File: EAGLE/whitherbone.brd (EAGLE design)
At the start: 86.4 x 54.6 mm, 222 parts, among them IC1 A4983, IC12 TPS2051BDGN, IC13 SN74AUC1G74, IC14 TPD4S012DRY, IC15 TPD4S012DRY, IC17 SN74LVC2G241DCUR, IC2 SN74LVC1G07DCK, IC4 7805T, IC7 IP4283CZ10-TBR, IC8 IP4283CZ10-TBR, IC9 TDA19988BHN/C1,557, J1 1-1747981-1, Q2 32.768kHz, Q4 24 MHz, T1 BSS138W-7-F, T3 BSS138W-7-F, T4 BSS138W-7-F, U1 OSD3358-512M-BSM, U2 SN74AHCT125PW, X2 SCHA5B0200, X4 10118192-0001LF

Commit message: Use version from Seeed
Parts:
- removed ANT1, ANT2: U.FL-R-SMT-1(10), GHI-Connectors:U.FL-R-SMT-1
- removed BT, BT1, PWR, USR0, USR1, USR2, USR3, WL: LTST-C191TBKT, GHI-BasicComponents:0603-LED
- removed FB4: 0.1 Ohm, 0805, GHI-BasicComponents:0805-RESISTOR
- removed IC13: SN74AUC1G74, GHI-IC:SM8-8(TI)
- removed IC14: TPD4S012DRY, GHI-IC:SON-6(TI)-DRY
- removed IC17: SN74LVC2G241DCUR, GHI-IC:VSSOP8(TI)
- removed IC2: SN74LVC1G07DCK, GHI-IC:SC70(TI-DCK)
- removed IC4: 7805T, linear:TO220H
- removed IC7, IC8: IP4283CZ10-TBR, GHI-IC:SOT1176-1(NXP)
- removed IC9: TDA19988BHN/C1,557, GHI-IC:SOT804-4(NXP)
- removed OSC1: ASDMB-24.576MHZ-LC-T, GHI2:OSCILLATOR-2.5X2.0-BBB
- removed OSC2: NZ2520SB-32.768KHZ-NSA3534C, GHI-IC:NZ2520S
- removed POWER, RESET: MINI_PUSHBUTTON, GHI2:MINI_PUSHBUTTON
- removed Q2: 32.768kHz, GHI2:CRYSTAL_3.2X1.5
- removed Q4: 24 MHz, GHI2:CRYSTAL_5X3.2MM
- removed R101: 10k, rcl:R0402
- removed R115, R118: 1.5k, 1%, rcl:R0402
- removed R119, R121: 10k, 1%, rcl:R0402
- removed R120: 27k, 1%, rcl:R0402
- removed R123, R76: 100k, 1%, rcl:R0402
- removed R23: 20K, SparkFun:0402-RES
- removed X1: (no value), GHI-Headers:TH-1X6
- removed X12: (no value), GHI-Connectors:PJ-102B_POWER_CON
- removed X3: (no value), GHI2:USB_HOST_HORIZONTAL_W/CHASSIS_GND
- removed X4: 10118192-0001LF, GHI-Connectors:10118192-0001LF(MICRO-USB-B-AMPHENOL-FCI)
- added ANT3, ANT4: (no value), Connector-new:U-FL3P-SMD-2.6X2.6X1.0MM
- added C22: 0.1uF, 6.3V, Discrete-new:C0402
- added C25, C26: 47pF, Discrete-new:C0402
- added C45, C65, C69, C76: 100nF, Discrete-new:C0402
- added C66: .1uF, 6.3V, Discrete-new:C0402
- added C67: 22nF, Discrete-new:C0402
- added C68: 100nF, Discrete-new:C0603
- added C70, C71: 47uF 25V, Discrete-new:ELECTRO-SMD-C-6MM
- added C72: 220nF, Discrete-new:C0402
- added C73: 100nF, Discrete-new:C0805
- added C74: DNI, Discrete-new:C0402
- added C75: 1uF 10V, Discrete-new:C0402
- added C77, C78, C80, C82, C83, C84: 10uF, Discrete-new:C0805
- added C79: 22uF, Discrete-new:ELECTRO-SMD-B-4.8MM
- added C81: 22uF 16V, Discrete-new:C1206
- added D10, D12, D13, D2, D3: DF2S6.8FS, Discrete-new:SOD-923
- added D11, D4, D5, D6, D7, D8, D9: (no value), Discrete-new:LED-0603
- added J2: (no value), Connector-new:H2-2.54
- added J3: 6p-2.54, OSD3358-BSP Ref Design:H6-2.54
- added J4: ST-HD-010, template:HDMI19P-0.5-15X12.15X6.18MM
- added J5: (no value), Connector-new:MICRO-SD9+4P-SMD-16.1X14.5X1.85MM
- added J6: DC Power Jack, For_Test_Albert:DC-404
- added J7: (no value), Connector-new:H4-3.5-14.0X7.0MM
- added J8: (no value), Connector-new:MICRO-USB5+5P-SMD-0.65-7.2X5.06MM
- added L1, L4: WPN201610MR47MT, Discrete-new:L201610
- added L2: 10uH, Discrete-new:L5040S
- added Q1: MMBT2907, Discrete-new:SOT-323
- added R106, R107, R108, R109, R112, R113: 33R, Discrete-new:R0402
- added R30, R51: 0R, Discrete-new:R0402
- added R31, R44: 22R, Discrete-new:R0402
- added R33: 0, 1%, Discrete-new:R0402
- added R33333, R48, R74, R77, R79, R97: 10k, Discrete-new:R0402
- added R36, R38: 1.5K, 1%, Discrete-new:R0402
- added R40: 5.6K 1%, Discrete-new:R0402
- added R41, R42: 100k 1%, Discrete-new:R0402
- added R45, R46: 2k, Discrete-new:R0402
- added R47: 33k, Discrete-new:R0402
- added R49, R50: 10K, Discrete-new:R0402
- added R54: 10k, 1%, Discrete-new:R0402
- added R59, R81, R82, R83: 100K, 1%, Discrete-new:R0402
- added R84: 3.3k, Discrete-new:R0402
- added R86, R89, R91: 10K, 1%, Discrete-new:R0402
- added R93: 510R 1%, Discrete-new:R0402
- added R94: 24k, Discrete-new:R0402
- added SW1, SW2: (no value), Discrete-new:BUTTON4P-SMD-4.5X3.2X2.5MM
- added TP11, TP21, TP22, TP23, TP24, TP3, TP4: TPB0,65, OSD3358-BSP Ref Design:TP_B0,65
- added TP20, TP25, TP27, TP28, TP29, TP30, TP31, TP32, TP9: (no value), Discrete-new:TP-D45MIL
- added TP26, TP5, TP6, TP7, TP8: TESTPAD/W_HOLE_1X1, OSD3358-BSP Ref Design:TESTPAD/W_HOLE_1X1
- added TP33: TPPAD1-13, testpad:P1-13
- added U10: (no value), IC-new:SOT-353
- added U11, U9: ESD-RCLAMP0524P, Discrete-new:ESD10P-0.5-2.5X1X0.58MM
- added U12: TL431, IC-new:SOT-23
- added U13: (no value), IC-new:5P-SMD-2X1.2X1MM
- added U3: MP1496DJ-LF-2, IC-new:SOT-23-8
- added U4: APX811, IC-new:SOT143-R
- added U5, U8: ETA3410, IC-new:DFN8G-0.5-2X2MM
- added U6: SN74LVC2G241_DCU_8, OSD3358-BSP Ref Design:DCU8
- added U7: IT66121FN, IC-new:QFN64-0.5-9X9MM
- added VIN: (no value), discrete:TP_4545
- added VR1: EVM3GSX50B14, Discrete-new:ADJR3-SMD-3.6X3.3MM
- added Y1: ABS07-32.768KHZ-T, OSD3358-BSP Ref Design:CRYSTAL_3.2X1.5
- added Y2: 7A-24.000MAAJ-T, OSD3358-BSP Ref Design:CRYSTAL-TXC-7A
- C1: value 10uF,10V -> 10uF; device rcl:C0603K -> Discrete-new:C0805
- C10: value .1uf -> 0.1uF, 6.3V; device SparkFun:0402-CAP -> Discrete-new:C0402
- C11: value 47uF DNP -> TLJB227M006R0500; device rcl:CT3528 -> Discrete-new:AVX-B
- C12: value 1uF,10V -> 18pF, 50V; device Seeed-Capacitor:C0402 -> Discrete-new:C0402
- C13, C14: value .1uf -> 100nF; device SparkFun:0402-CAP -> Discrete-new:C0402
- C15, C18: value .1uf -> 10uF; device SparkFun:0402-CAP -> Discrete-new:C0805
- C16: value 2.2uF, 6.3V -> 100nF; device rcl:C0603K -> Discrete-new:C0402
- C17: value .22uF -> 100nF; device SparkFun:0402-CAP -> Discrete-new:C0402
- C19: value 1uF,10V -> 10uF; device Seeed-Capacitor:C0402 -> Discrete-new:C0805
- C2: value .1uF, 6.3V -> DNI; device rcl:C0402K -> Discrete-new:C0402
- C20: value 10uF, 6.3V -> 10uF; device rcl:C0603K -> Discrete-new:C0805
- C21: value 1uF,10V -> 10uF, 10V; device Seeed-Capacitor:C0402 -> Discrete-new:C0805
- C23: value 47uF DNP -> 47pF; device rcl:CT3528 -> Discrete-new:C0402
- C24: value .1uF, 6.3V -> 47pF; device rcl:C0402K -> Discrete-new:C0402
- C27, C28, C29, C30, C31, C32, C33, C34, C35, C36, C37, C38: value 47pF, 6.3V -> 47pF; device rcl:C0402K -> Discrete-new:C0402
- C3, C6: value 18pF, 50V -> 0.1uF, 6.3V; device rcl:C0402K -> Discrete-new:C0402
- C39, C40, C41: value 47pF, 6.3V -> 10uF; device rcl:C0402K -> Discrete-new:C0805
- C4, C5: device rcl:C0402K -> Discrete-new:C0402
- C42: value 47pF, 6.3V -> 1uF; device rcl:C0402K -> Discrete-new:C0402
- C43, C44, C47, C48, C49, C50, C51, C63: value .1uF, 6.3V -> 100nF; device rcl:C0402K -> Discrete-new:C0402
- C46, C60: value 10pF -> 100nF; device rcl:C0402K -> Discrete-new:C0402
- C52, C53: value .1uF, 6.3V -> 47uF DNP; device rcl:C0402K -> Discrete-new:C1206
- C54: value 2.2uF, 6.3V -> 220uF; device rcl:C0603K -> Discrete-new:AVX-E
- C55, C56: value 2.2uF, 6.3V -> 10pF; device rcl:C0603K -> Discrete-new:C0402
- C57: value 2.2uF, 6.3V -> 10uF; device rcl:C0603K -> Discrete-new:C0805
- C58: value .1uF, 6.3V -> 1uF; device rcl:C0402K -> Discrete-new:C0402
- C59: value .1uF, 6.3V -> DNP; device rcl:C0402K -> Discrete-new:C0402
- C61: value 10uF, 6.3V -> 100nF; device rcl:C0603K -> Discrete-new:C0402
- C62: value 220uF 6.3V -> 1uF; device rcl:D/7343-31W -> Discrete-new:C0603
- C64: value 1uF, 6.3V -> 1uF; device rcl:C0402K -> Discrete-new:C0402
- C7: value 47uF,50V -> 18pF, 50V; device resistor:PANASONIC_F -> Discrete-new:C0402
- C8: value 1uF -> 1nF; device rcl:C0402K -> Discrete-new:C0402
- C9: value 100nF,50V -> 0.1uF, 6.3V; device Seeed-Capacitor:C0805 -> Discrete-new:C0402
- D1: value RB751V40,115 -> (none); device GHI-BasicComponents:SOD323(NXP)REFLOW -> Discrete-new:LED-0603
- F1: value 1206L025YR -> 100mA MF-FSMF010X; device inductor-neosid:SM-1206 -> Discrete-new:F0603
- FB1, FB6, FB7, FB8: value 1k BLM15AG102SN1D -> BLM15PD121SN1D; device rcl:R0402 -> Discrete-new:L0402
- FB2: value 2.5k Ohm (BLM18BD252SN1D) -> BLM15PD121SN1D; device GHI-BasicComponents:0805-RESISTOR -> Discrete-new:L0402
- FB3: device GHI-BasicComponents:0805-RESISTOR -> Discrete-new:L0805
- FB5: value 1k BLM15AG102SN1D -> 0.1 Ohm, 0805; device rcl:R0402 -> Discrete-new:L0805
- FUD1, FUD2, FUD3, FUD4, FUD5, FUD6: device GHI:FIDUCIAL_40MIL -> OSD3358-BSP Ref Design:FIDUCIAL_40MIL
- IC1: device SparkFun:QFN-28-5MM -> IC-new:QFN-28-5MM
- IC12: device GHI-IC:MSOP-POWER.PAD-8(TI) -> IC-new:MSOP8-0.65-3X3MM
- IC15: device GHI-IC:SON-6(TI)-DRY -> IC-new:SON6-0.5-1.45X1X0.55MM
- J1: value 1-1747981-1 -> (none); device 1-1747981-1:TE_1-1747981-1 -> Connector-new:H2-2.54
- MGT1, MGT2, MGT3, MGT4: device BeagleBoneBlack:MOUNTING_HOLE -> OSD3358-BSP Ref Design:MOUNTING_HOLE
- MOD1: device GHI-IC:MOC-100(TI) -> moudle-new:MODULE100P-0.7-13.5X13.2MM
- R1: value 10k, 1% -> 10K, 1%; device rcl:R0402 -> Discrete-new:R0402
- R10: value .11 -> 0, 1%; device SparkFun:R2010 -> Discrete-new:R0402
- R100, R104, R96: value 1k -> 10k; device rcl:R0402 -> Discrete-new:R0402
- R102, R103, R105, R111, R122, R124, R125: device rcl:R0402 -> Discrete-new:R0402
- R11: value 20K -> 0, 1%; device SparkFun:0402-RES -> Discrete-new:R0402
- R110: value 33 -> 33R; device rcl:R0402 -> Discrete-new:R0402
- R114: value 0, 1% -> 1k; device rcl:R0402 -> Discrete-new:R0402
- R12, R13: value 20K -> 1.5K, 1%; device SparkFun:0402-RES -> Discrete-new:R0402
- R14: value 20K -> 22k 1%; device SparkFun:0402-RES -> Discrete-new:R0402
- R140, R141, R142, R143: value 33, 5% -> 33R; device rcl:R0402 -> Discrete-new:R0402
- R15: value 20K -> 40.2K, 1%; device SparkFun:0402-RES -> Discrete-new:R0402
- R16: value 10K -> 0, 1%; device SparkFun:TRIMPOT-3MM -> Discrete-new:R0402
- R17: value .1, 0805 -> DNP; device rcl:R0805 -> Discrete-new:R0402
- R18: value .11 -> 4.75K, 1%; device SparkFun:R2010 -> Discrete-new:R0402
- R19: value 10k, 1% -> 10k; device rcl:R0402 -> Discrete-new:R0402
- R2, R3: value 10k, 1% -> 1k; device rcl:R0402 -> Discrete-new:R0402
- R20: value 20K -> 10K, 1%; device SparkFun:0402-RES -> Discrete-new:R0402
- R21: value 20K -> 499; device SparkFun:0402-RES -> Discrete-new:R0402
- R22: value 20K -> 4.75K, 1%; device SparkFun:0402-RES -> Discrete-new:R0402
- R24: value 10k, 1% -> 1M, 1%, DNI; device rcl:R0402 -> Discrete-new:R0402
- R25: value 2.49K -> 0, 1%; device SparkFun:0402-RES -> Discrete-new:R0402
- R26, R35, R37: value 0, 1% -> 1.5K, 1%; device rcl:R0402 -> Discrete-new:R0402
- R27: value 0, 1% -> 100K, 1%; device rcl:R0402 -> Discrete-new:R0402
- R28: value 47k, 1% -> 0R; device rcl:R0402 -> Discrete-new:R0402
- R29: value 22k, 1% -> 0R; device rcl:R0402 -> Discrete-new:R0402
- R32: value 10k, 1% -> 1M, 1%; device rcl:R0402 -> Discrete-new:R0402
- R34: value 22 -> 10k; device rcl:R0402 -> Discrete-new:R0402
- R39: value 0, 1% -> 10k; device rcl:R0402 -> Discrete-new:R0402
- R4: value 10k, 1% -> 22R; device rcl:R0402 -> Discrete-new:R0402
- R43: value 4.75k, 1% -> 22R; device rcl:R0402 -> Discrete-new:R0402
- R5: value 10k, 1% -> 0, 1%; device rcl:R0402 -> Discrete-new:R0402
- R52: value 4.75k, 1% -> DNP; device rcl:R0402 -> Discrete-new:R0402
- R53, R55: value 4.75k, 1% -> 100K, 1%; device rcl:R0402 -> Discrete-new:R0402
- R56: value DNP 1M, 1% -> 100K, 1%; device rcl:R0402 -> Discrete-new:R0402
- R57, R58, R61, R63, R67, R71: value 100k, 1% -> 100K, 1%; device rcl:R0402 -> Discrete-new:R0402
- R6: value 10k, 1% -> 100K, 1%, DNI; device rcl:R0402 -> Discrete-new:R0402
- R60, R62, R68: value 33, 5% -> 100K, 1%; device rcl:R0402 -> Discrete-new:R0402
- R64: value 33, 5% -> 100k; device rcl:R0402 -> Discrete-new:R0402
- R65: value 100k, 1% -> 0.1R; device rcl:R0402 -> Discrete-new:R1206
- R66: value 33, 5% -> 0.1R; device rcl:R0402 -> Discrete-new:R1206
- R69: value 100k, 1% -> 10R; device rcl:R0402 -> Discrete-new:R0402
- R7: value 10k, 1% -> 0R; device rcl:R0402 -> Discrete-new:R1206
- R70: value 33, 5% -> 10K; device rcl:R0402 -> Discrete-new:R0402
- R72: value 33, 5% -> 10k; device rcl:R0402 -> Discrete-new:R0402
- R73, R75, R78, R80: value 100k, 1% -> 10k; device rcl:R0402 -> Discrete-new:R0402
- R8: value 1M, 1% -> 1K, 1%; device rcl:R0402 -> Discrete-new:R0402
- R85: value 100k, 1% -> 2.7k 1%; device rcl:R0402 -> Discrete-new:R0402
- R87, R88: value 100k, 1% -> 10K, 1%; device rcl:R0402 -> Discrete-new:R0402
- R9: value 1k -> 100k 1%; device rcl:R0402 -> Discrete-new:R0402
- R90, R92: value 1k -> 10K, 1%; device rcl:R0402 -> Discrete-new:R0402
- R98, R99: value 10k -> 10K; device rcl:R0402 -> Discrete-new:R0402
- T1, T3, T4: device GHI Transistors:SOT-323(DIODES) -> Discrete-new:SOT-323
- TP1: value TESTPAD/W_HOLE_1X1 -> TPB0,65; device GHI2:TESTPAD/W_HOLE_1X1 -> OSD3358-BSP Ref Design:TP_B0,65
- TP12, TP13, TP14, TP15, TP16: value PTR1B1,27 -> TPB0,65; device testpad:B1,27 -> OSD3358-BSP Ref Design:TP_B0,65
- TP17, TP18, TP19: value PTR1B1,27 -> (none); device testpad:B1,27 -> Discrete-new:TP-D45MIL
- TP2: value TPPAD1-13 -> TPB0,65; device testpad:P1-13 -> OSD3358-BSP Ref Design:TP_B0,65
- U1: value OSD3358-512M-BSM -> (none); device PocketBeagle:OSD335X-BGA-256 -> IC-new:BGA256-1.27-21X21MM
- U2: value SN74AHCT125PW -> (none); device SN74AHCT125PW:SOP65P640X120-14N -> IC-new:SON6-0.5-1.45X1X0.55MM
- X2: value SCHA5B0200 -> (none); device GHI-Connectors:SCHA5B0200 -> GHI2:USB_HOST_HORIZONTAL_W/CHASSIS_GND
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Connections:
- net N$5 renamed AIN7
- removed net 12MHZ: FB6.2, IC9.27
- removed net 12M_LOOP: IC13.2, IC13.3
- removed net 32.768KHZ: MOD1.36, OSC2.3
- removed net DVI_5V: F1.1, J1.2, R115.1, R118.1
- removed net EXT_SWING: IC9.34, R119.1
- removed net HDMI.DSCL: IC9.33, J1.5, R115.2
- removed net HDMI.DSDA: IC9.32, J1.4, R118.2
- removed net HDMI_1V8: C50.1, C51.1, C52.1, C53.1, C54.1, C55.1, C56.1, C57.1, FB2.2, IC9.14, IC9.29, IC9.35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
- removed net HDMI_AUDCLK: R110.2, U1.C4
- removed net HDMI_AUDCLK_DIS#: OSC1.1, U1.T16
- removed net LCD.CLOCK: IC9.4, R34.1
- removed net LCD.D0.B0--B3: C42.1, IC9.15, R87.2, U1.G3
- removed net LCD.D1.B1--B4: C41.1, IC9.13, R85.2, U1.G2
- removed net LCD.D10.G5--G7: C32.1, IC9.64, R67.2, U1.K2
- removed net LCD.D11.R0--R3: C31.1, IC9.60, R65.2, U1.K1
- removed net LCD.D12.R1--R4: C30.1, IC9.59, R63.2, U1.L3
- removed net LCD.D13.R2--R5: C29.1, IC9.58, R61.2, U1.L2
- removed net LCD.D14.R3--R6: C28.1, IC9.57, R58.1, U1.L1
- removed net LCD.D15.R4--R7: C27.1, IC9.56, R57.2, U1.M3
- removed net LCD.D2.B2--B5: C40.1, IC9.12, R88.1, U1.G1
- removed net LCD.D3.B3--B6: C39.1, IC9.11, R80.1, U1.H3
- removed net LCD.D4.B4--B7: C38.1, IC9.10, R78.1, U1.H2
- removed net LCD.D5.G0--G2: C37.1, IC9.7, R76.1, U1.H1
- removed net LCD.D6.G1--G3: C36.1, IC9.6, R75.2, U1.J3
- removed net LCD.D7.G2--G4: C35.1, IC9.3, R73.2, U1.J2
- removed net LCD.D8.G3--G5: C34.1, IC9.2, R71.2, U1.J1
- removed net LCD.D9.G4--G6: C33.1, IC9.1, R69.2, U1.K3
- removed net LCD.ENABLE: IC9.20, R39.1
- removed net LCD.HSYNC: IC9.22, R37.1
- removed net LCD.VSYNC: IC9.21, R35.1
- removed net MCU.LCD.CLK: R34.2, U1.F1
- removed net MCU.LCD.EN: R39.2, U1.E1
- removed net MCU.LCD.HS: R37.2, U1.F2
- removed net MCU.LCD.VS: R35.2, U1.F3
- removed net N$12: C5.2, C6.2
- removed net N$4: PWR.K, R55.2
- removed net N$58: FB6.1, IC13.5
- removed net RX<-TX: IC17.3, X1.5
- removed net SD.CD: R7.1, U1.C14, X2.CD
- removed net SD.CLK: R3.1, U1.B15, X2.5
- removed net SD.CMD: R4.1, U1.B16, X2.3
- removed net SD.D0: R2.1, U1.A16, X2.7
- removed net SD.D1: R1.1, U1.A15, X2.8
- removed net SD.D2: R6.1, U1.C16, X2.1
- removed net SD.D3: R5.1, U1.C15, X2.2
- removed net SYS_RESET#: C16.1, IC2.4, R32.2, RESET.3, RESET.4, U1.R11
- removed net TEST: IC9.49, R114.2
- removed net TX->RX: IC17.2, R123.1, X1.4
- removed net TX0+: IC8.5, IC9.40, J1.13
- removed net TX0-: IC8.4, IC9.39, J1.11
- removed net TX1+: IC7.2, IC9.43, J1.16
- removed net TX1-: IC7.1, IC9.42, J1.14
- removed net TX2+: IC7.5, IC9.45, J1.19
- removed net TX2-: IC7.4, IC9.44, J1.17
- removed net TXC+: IC8.2, IC9.38, J1.10
- removed net TXC-: IC8.1, IC9.37, J1.8
- removed net UART0_RXD: IC17.6, U1.A12
- removed net UART0_TXD: IC17.5, U1.B12
- removed net USB.CLIENT.D+: IC14.1, X4.D+
- removed net USB.CLIENT.D-: IC14.2, X4.D-
- removed net USB.CLIENT.ID: IC14.3, X4.ID
- removed net USB.HOST.D+: IC15.1, X3.3
- removed net USB.HOST.D-: IC15.2, X3.2
- removed net USB_DC: C59.1, IC14.6, R26.2, U1.P9, U1.R9, U1.T9, X4.VBUS
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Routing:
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- added copper zone on layer 1, net SYS_RTC_1P8V
- added copper zone on layer 1, net SYS_VDD1_3P3V
- added copper zone on layer 1, net SYS_VDD2_3P3V
- added copper zone on layer 1, net SYS_VDD3_3P3V
- added copper zone on layer 1, net SYS_VDD_1P8V
- added copper zone on layer 1, net SYS_VOUT
- added copper zone on layer 1, net VDD_BAT
- added copper zone on layer 1, net VDD_USB_5V
- removed copper zone on layer 1, net 1.8V-WIFI
- removed copper zone on layer 1, net 3.3V-WIFI
- removed copper zone on layer 1, net 5V_IN
- removed copper zone on layer 16, net 5V_IN
- removed copper zone on layer 16, net CGND
- removed copper zone on layer 16, net DVI_5V
- removed copper zone on layer 15, net GND
- removed copper zone on layer 16, net GND
- removed copper zone on layer 15, net N$25
- removed copper zone on layer 2, net N$25
- removed copper zone on layer 16, net SELECT_5V
- removed copper zone on layer 1, net SYS_5V
- removed copper zone on layer 16, net SYS_5V
- removed copper zone on layer 1, net USB_DC
- removed copper zone on layer 16, net USB_DC
- removed copper zone on layer 16, net VBUS.HOST
- removed copper zone on layer 16, net VBUS.OUT
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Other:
- board size 86.4 x 54.6 mm -> 101.6 x 101.6 mm
- board text removed: "+"
- board text removed: "5V"
- board text removed: "A5"
- board text removed: "BeagleBone Black Wireless"
- board text removed: "OSD3358"

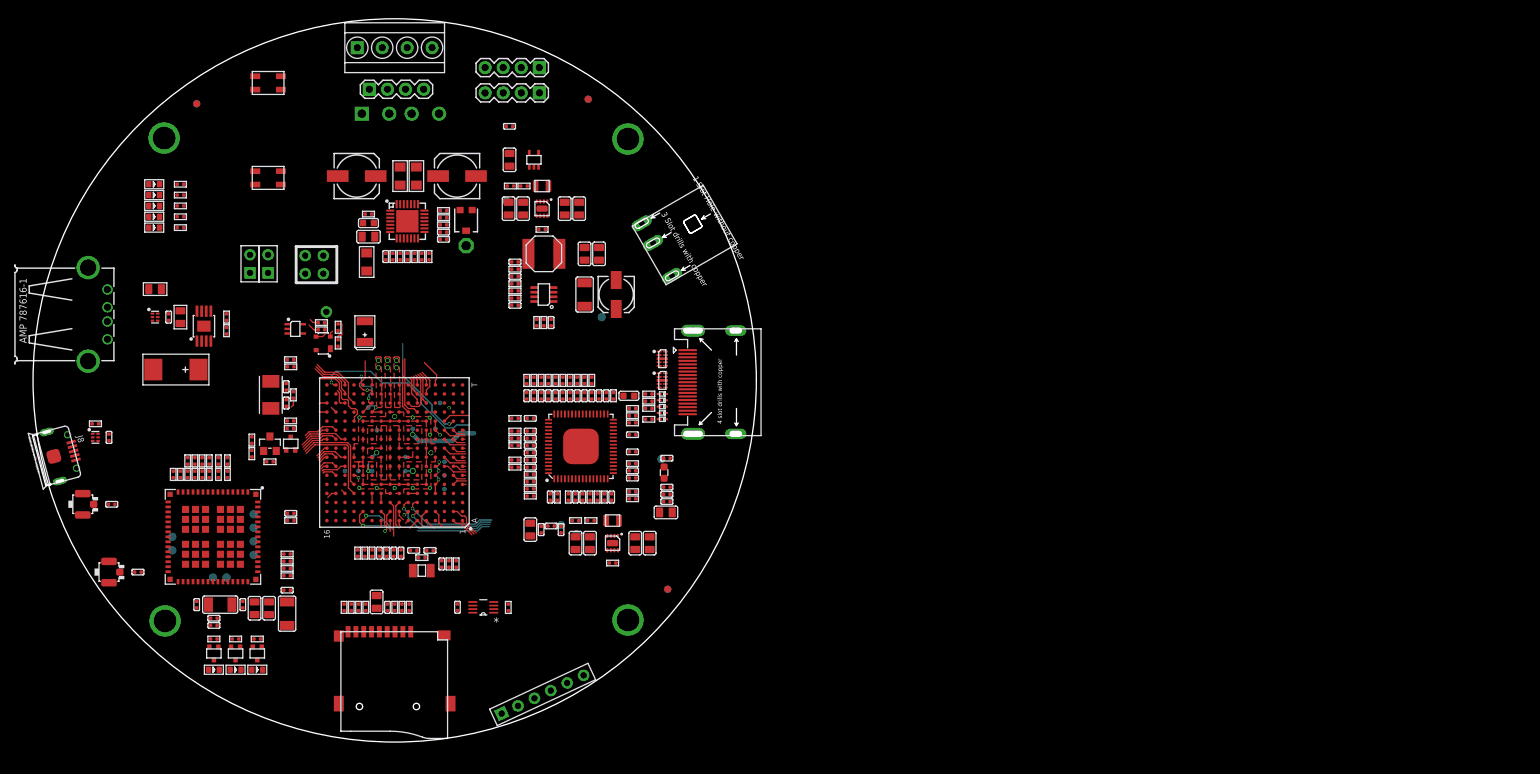
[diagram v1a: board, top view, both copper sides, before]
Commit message: Update to latest from Seeed
* Layout complete
* Added mechanical drawing (DXF) for board
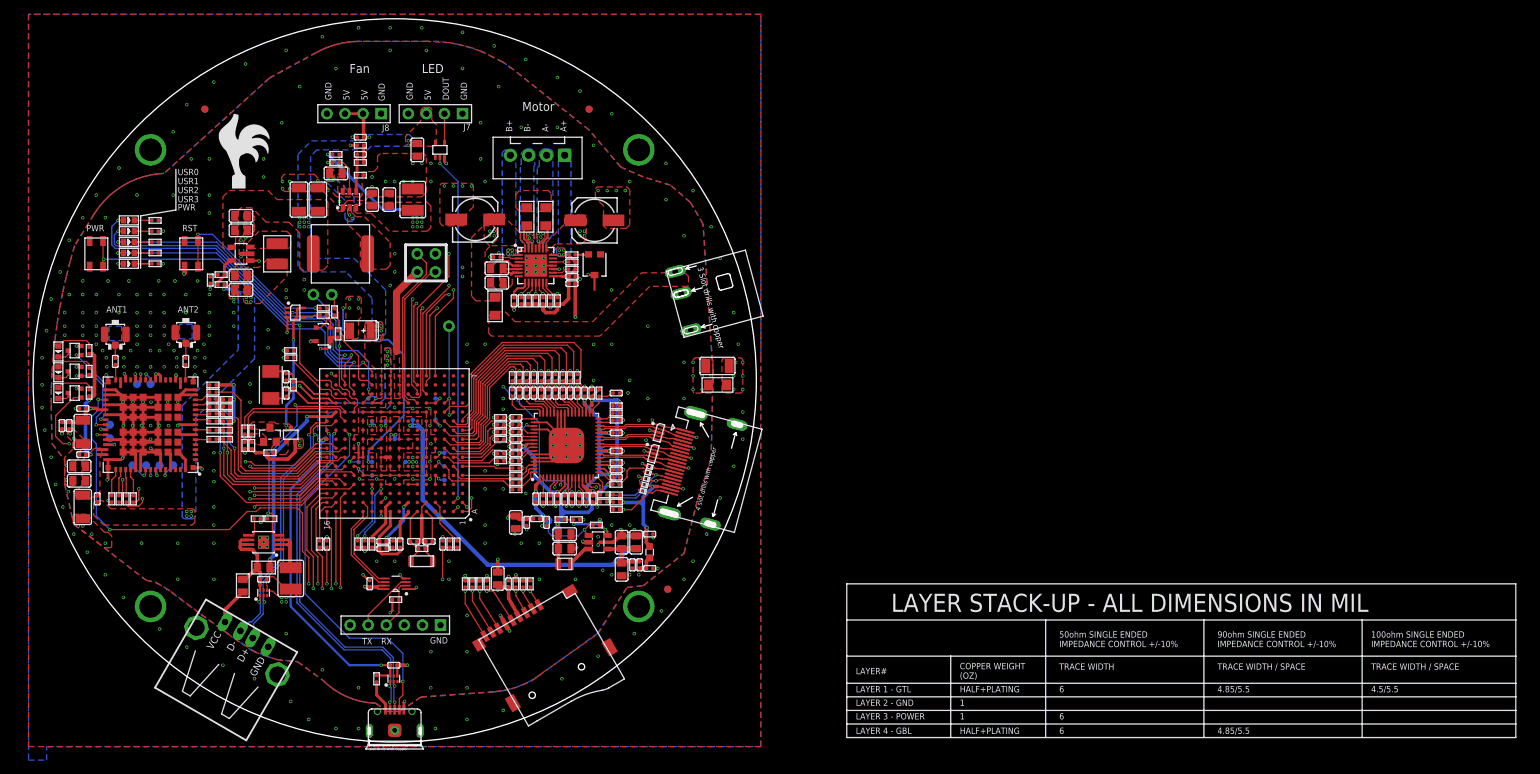
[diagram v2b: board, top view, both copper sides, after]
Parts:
- removed ANT3, ANT4: (no value), Connector-new:U-FL3P-SMD-2.6X2.6X1.0MM
- removed FB1, FB2, FB6, FB7, FB8: BLM15PD121SN1D, Discrete-new:L0402
- removed FB3: 150 Ohm 800mA, Discrete-new:L0805
- removed FB5: 0.1 Ohm, 0805, Discrete-new:L0805
- removed IC12: TPS2051BDGN, IC-new:MSOP8-0.65-3X3MM
- removed IC15: TPD4S012DRY, IC-new:SON6-0.5-1.45X1X0.55MM
- removed JP1, JP3: (no value), SparkFun:1X04
- removed JP5: (no value), BigEasyDriver_v11:SCREWTERMINAL-3.5MM-4_LOCK
- removed MOD1: WL1835MODGBMOCT, moudle-new:MODULE100P-0.7-13.5X13.2MM
- removed R122: 0, 1%, Discrete-new:R0402
- removed R124, R125: 1k, Discrete-new:R0402
- removed R140, R141, R142, R143: 33R, Discrete-new:R0402
- removed R33333: 10k, Discrete-new:R0402
- removed T1, T3, T4: BSS138W-7-F, Discrete-new:SOT-323
- removed TP33: TPPAD1-13, testpad:P1-13
- removed VIN: (no value), discrete:TP_4545
- removed X2: (no value), GHI2:USB_HOST_HORIZONTAL_W/CHASSIS_GND
- removed Y2: 7A-24.000MAAJ-T, OSD3358-BSP Ref Design:CRYSTAL-TXC-7A
- added ANT1, ANT2: RECE.20279.001E.01, Connector-new:U-FL3P-SMD-2.6X2.6X1.0MM
- added IC2: TPD4S012DRYR, IC-new:SON6-0.5-1.45X1X0.55MM
- added L10: WPN201610MR47MT, Discrete-new:L201610
- added L3: IHLP3232DZER100M01, Discrete-new:INT2-7.268-8.64X8.18X4MM
- added L5: BLM21PG331SN1D, Discrete-new:L0805
- added L6: LQH44PN1R0NP0L, Discrete-new:L4.4X3.0MM
- added L7, L8, L9: BLM15PD121SN1D, Discrete-new:L0402
- added Q2, Q3: BSS138W-7-F, Discrete-new:SOT-323
- added Q4: MMBT2907A, Discrete-new:SOT-323
- added R101: DNP, Discrete-new:R0402
- added R115, R95: 22R, Discrete-new:R0402
- added R116, R117, R118, R23: 0R, Discrete-new:R0402
- added R76: 51k 1%, Discrete-new:R0402
- added TP10, TP34: (no value), Discrete-new:TP-D65/35MIL
- added U14: ESD-RCLAMP0524P, Discrete-new:ESD10P-0.5-2.5X1X0.58MM
- added U16: TLV62569DBVT, IC-new:SOT-23-5
- added X1: ST3215SB32768H5HPWAA, Discrete-new:X2-SMD-3.2X1.5X0.55MM
- C1: value 10uF -> TLJB227M006R0500; device Discrete-new:C0805 -> Discrete-new:AVX-B
- C10, C9: value 0.1uF, 6.3V -> 10pF
- C11: value TLJB227M006R0500 -> 1nF 1000V; device Discrete-new:AVX-B -> Discrete-new:C1206
- C12: value 18pF, 50V -> 18pF 50V
- C13, C14: value 100nF -> 18pF 50V
- C15: value 10uF -> 18pF 50V; device Discrete-new:C0805 -> Discrete-new:C0402
- C16: value 100nF -> 100uF 16V; device Discrete-new:C0402 -> Discrete-new:C1210
- C17: value 100nF -> 100nF 50V; device Discrete-new:C0402 -> Discrete-new:C0805
- C18, C82, C83: value 10uF -> 10uF 25V
- C19: value 10uF -> 100nF 50V
- C2: value DNI -> 1uF 10V
- C20, C77, C78, C80: value 10uF -> 100nF 25V; device Discrete-new:C0805 -> Discrete-new:C0402
- C21: value 10uF, 10V -> 22uF 16V; device Discrete-new:C0805 -> Discrete-new:C1206
- C22: value 0.1uF, 6.3V -> 22uF 16V; device Discrete-new:C0402 -> Discrete-new:C1206
- C23: value 47pF -> 75pF 50V
- C24: value 47pF -> 100uF 16V; device Discrete-new:C0402 -> Discrete-new:C1210
- C25, C27, C28, C31, C34: value 47pF -> 100nF 25V
- C26, C38: value 47pF -> 1uF 10V
- C29, C30, C32, C33, C35, C36: value 47pF -> 10uF 25V; device Discrete-new:C0402 -> Discrete-new:C0805
- C3: value 0.1uF, 6.3V -> 47uF DNP; device Discrete-new:C0402 -> Discrete-new:C1206
- C37: value 47pF -> DNI
- C39, C41, C57: value 10uF -> 33pF 50V; device Discrete-new:C0805 -> Discrete-new:C0402
- C4, C5: value 18pF, 50V -> 10uF 25V; device Discrete-new:C0402 -> Discrete-new:C0805
- C40: value 10uF -> DNI; device Discrete-new:C0805 -> Discrete-new:C0402
- C42, C58: value 1uF -> 33pF 50V
- C43, C45, C46, C47, C49, C50, C60: value 100nF -> 33pF 50V
- C44, C61, C63, C65, C69, C76: value 100nF -> 100nF 25V
- C48, C51: value 100nF -> 47uF 25V; device Discrete-new:C0402 -> Discrete-new:ELECTRO-SMD-C-6MM
- C52: value 47uF DNP -> 33pF 50V; device Discrete-new:C1206 -> Discrete-new:C0402
- C53: value 47uF DNP -> 100nF 25V; device Discrete-new:C1206 -> Discrete-new:C0402
- C54: value 220uF -> 33pF 50V; device Discrete-new:AVX-E -> Discrete-new:C0402
- C55: value 10pF -> 33pF 50V
- C56: value 10pF -> 100nF 50V; device Discrete-new:C0402 -> Discrete-new:C0805
- C59: value DNP -> 33pF 50V
- C6: value 0.1uF, 6.3V -> 100nF 25V
- C62: value 1uF -> 100nF 25V; device Discrete-new:C0603 -> Discrete-new:C0402
- C64: value 1uF -> 100nF 25V
- C66: value .1uF, 6.3V -> 100nF 25V
- C67: value 22nF -> 220nF
- C68: value 100nF -> 100nF 50V; device Discrete-new:C0603 -> Discrete-new:C0805
- C7: value 18pF, 50V -> 47uF DNP; device Discrete-new:C0402 -> Discrete-new:C1206
- C70: value 47uF 25V -> 10uF 25V; device Discrete-new:ELECTRO-SMD-C-6MM -> Discrete-new:C0805
- C71: value 47uF 25V -> 100nF 25V; device Discrete-new:ELECTRO-SMD-C-6MM -> Discrete-new:C0402
- C72: value 220nF -> 100nF 25V
- C73: value 100nF -> 100nF 25V; device Discrete-new:C0805 -> Discrete-new:C0402
- C74: value DNI -> 10uF 25V; device Discrete-new:C0402 -> Discrete-new:C0805
- C75: value 1uF 10V -> 10uF 25V; device Discrete-new:C0402 -> Discrete-new:C0805
- C79: value 22uF -> 10uF 25V; device Discrete-new:ELECTRO-SMD-B-4.8MM -> Discrete-new:C0805
- C8: value 1nF -> 1uF 10V
- C81: value 22uF 16V -> 100nF 25V; device Discrete-new:C1206 -> Discrete-new:C0402
- C84: value 10uF -> 1uF; device Discrete-new:C0805 -> Discrete-new:C0402
- D1, D5, D6, D7, D8: value (none) -> Red
- D11, D9: value (none) -> DF2S6.8FS; device Discrete-new:LED-0603 -> Discrete-new:SOD-923
- D2, D3: value DF2S6.8FS -> Green; device Discrete-new:SOD-923 -> Discrete-new:LED-0603
- D4: value (none) -> Green
- F1: value 100mA MF-FSMF010X -> MF-FSMF010X
- IC1: value A4983 -> TPD4S012DRYR; device IC-new:QFN-28-5MM -> IC-new:SON6-0.5-1.45X1X0.55MM
- J1: value (none) -> ST-USB-01H2; device Connector-new:H2-2.54 -> Connector-new:MICRO-USB5+5P-SMD-0.65-7.2X5.06MM
- J2: value (none) -> DC-044; device Connector-new:H2-2.54 -> Connector-new:DCJ3P-11.6X9.6X7.0MM
- J3: value 6p-2.54 -> ST-TF-003J; device OSD3358-BSP Ref Design:H6-2.54 -> Connector-new:MICRO-SD9+4P-SMD-16.1X14.5X1.85MM
- J4: value ST-HD-010 -> 6p-2.54 DNP; device template:HDMI19P-0.5-15X12.15X6.18MM -> OSD3358-BSP Ref Design:H6-2.54
- J5: value (none) -> WY-1223; device Connector-new:MICRO-SD9+4P-SMD-16.1X14.5X1.85MM -> Connector-new:H4-2.54-10.2X5.6MM
- J6: value DC Power Jack -> ST-HD-010; device For_Test_Albert:DC-404 -> template:HDMI19P-0.5-15X12.15X6.18MM
- J7: value (none) -> 2510S-4P(T); device Connector-new:H4-3.5-14.0X7.0MM -> Connector-new:H4-2.54
- J8: value (none) -> 2510S-4P(T); device Connector-new:MICRO-USB5+5P-SMD-0.65-7.2X5.06MM -> Connector-new:H4-2.54
- JP2: value (none) -> ST-USB-003A; device SparkFun:1X04 -> Connector-new:USB4+2-2.0-90D
- L1: value WPN201610MR47MT -> BLM15PD121SN1D; device Discrete-new:L201610 -> Discrete-new:L0402
- L2: value 10uH -> BLM15PD121SN1D; device Discrete-new:L5040S -> Discrete-new:L0402
- L4: value WPN201610MR47MT -> BLM21PG331SN1D; device Discrete-new:L201610 -> Discrete-new:L0805
- Q1: value MMBT2907 -> BSS138W-7-F
- R1: value 10K, 1% -> 1.5k 1%
- R10: value 0, 1% -> 10k
- R102, R103: value 10k -> 22R
- R104, R105: value 10k -> 2k
- R106, R108, R109, R112: value 33R -> 10k
- R107: value 33R -> 33k
- R11, R5: value 0, 1% -> 1k
- R110: value 33R -> 0.1R; device Discrete-new:R0402 -> Discrete-new:R1206
- R111: value DNP 10k -> 0.1R; device Discrete-new:R0402 -> Discrete-new:R1206
- R113: value 33R -> 100k 1%
- R114: value 1k -> 100k 1%
- R12: value 1.5K, 1% -> 1k
- R13, R26: value 1.5K, 1% -> 33R
- R14: value 22k 1% -> 33R
- R15: value 40.2K, 1% -> 33R
- R16, R25: value 0, 1% -> 33R
- R17: value DNP -> 499R
- R18: value 4.75K, 1% -> 1.5k 1%
- R19: value 10k -> 33R
- R2: value 1k -> 1.5k 1%
- R20: value 10K, 1% -> 40.2k 1%
- R21: value 499 -> 10k 1%
- R22: value 4.75K, 1% -> 33R
- R24: value 1M, 1%, DNI -> 0R
- R27: value 100K, 1% -> 33R
- R28, R29: value 0R -> 33R
- R3: value 1k -> 10k 1%
- R30: value 0R -> DNP 10k
- R31: value 22R -> 1k
- R32: value 1M, 1% -> 100K, 1%, DNI
- R33: value 0, 1% -> 100k 1%
- R34, R39, R80: value 10k -> 100k 1%
- R35, R36, R37, R38: value 1.5K, 1% -> 100k 1%
- R4: value 22R -> 10k
- R40: value 5.6K 1% -> 100k 1%
- R43, R44: value 22R -> 100k 1%
- R45, R46: value 2k -> 100k 1%
- R47: value 33k -> 0R
- R48, R97: value 10k -> 0R; device Discrete-new:R0402 -> Discrete-new:R1206
- R49, R50: value 10K -> 100k 1%
- R51: value 0R -> 1.5k 1%
- R52: value DNP -> 1.5k 1%
- R53: value 100K, 1% -> 1.5k 1%
- R54: value 10k, 1% -> 1.5k 1%
- R55: value 100K, 1% -> 1M 1%
- R56: value 100K, 1% -> 1M, 1%, DNI
- R57: value 100K, 1% -> 560k 1%
- R58, R60: value 100K, 1% -> 100k 1%
- R59: value 100K, 1% -> 49.9R 1%
- R6: value 100K, 1%, DNI -> 10k
- R61: value 100K, 1% -> 13.3k 1%
- R62: value 100K, 1% -> 10k 1%
- R63: value 100K, 1% -> 0R
- R64: value 100k -> 0R
- R65, R66: value 0.1R -> 0R; device Discrete-new:R1206 -> Discrete-new:R0402
- R67, R68, R71, R81, R82, R83: value 100K, 1% -> 10k
- R69: value 10R -> 10k 1%
- R7: value 0R -> 10k; device Discrete-new:R1206 -> Discrete-new:R0402
- R70: value 10K -> 10k 1%
- R77: value 10k -> 1.3k 1%
- R78: value 10k -> 240k 1%
- R79, R96: value 10k -> 1k
- R8: value 1K, 1% -> 10k
- R84: value 3.3k -> 10k
- R85: value 2.7k 1% -> 0R
- R86: value 10K, 1% -> DNP
- R87, R88, R89, R90, R91, R92: value 10K, 1% -> 10k
- R9: value 100k 1% -> 10k
- R93: value 510R 1% -> 10k
- R94: value 24k -> 10k
- R98: value 10K -> 10k
- R99: value 10K -> 5.6K 1%
- SW1, SW2: value (none) -> SKRPABE010
- TP1: value TPB0,65 -> (none); device OSD3358-BSP Ref Design:TP_B0,65 -> discrete:TP_4545
- TP9: value (none) -> TPB0,65; device Discrete-new:TP-D45MIL -> OSD3358-SM-RED Platform:TP_B0,65
- U1: value (none) -> OSD3358-512M-BSM
- U10: value (none) -> SN74LVC2G241DCUR; device IC-new:SOT-353 -> IC-new:DCU8
- U11: value ESD-RCLAMP0524P -> IT66121FN; device Discrete-new:ESD10P-0.5-2.5X1X0.58MM -> IC-new:QFN64-0.5-9X9MM
- U12: value TL431 -> A4988SETTR-T; device IC-new:SOT-23 -> IC-new:QFN-28-5MM
- U13: value (none) -> ESD-RCLAMP0524P; device IC-new:5P-SMD-2X1.2X1MM -> Discrete-new:ESD10P-0.5-2.5X1X0.58MM
- U2: value (none) -> SN74LVC1G07DCKR; device IC-new:SON6-0.5-1.45X1X0.55MM -> IC-new:5P-SMD-2X1.2X1MM
- U3: value MP1496DJ-LF-2 -> ATL431AIDBZR; device IC-new:SOT-23-8 -> IC-new:SOT-23
- U4: value APX811 -> WL1835MODGBMOCT; device IC-new:SOT143-R -> moudle-new:MODULE100P-0.7-13.5X13.2MM
- U5: value ETA3410 -> APX811-44UG-7; device IC-new:DFN8G-0.5-2X2MM -> IC-new:SOT143-R
- U6: value SN74LVC2G241_DCU_8 -> TPS54302; device OSD3358-BSP Ref Design:DCU8 -> IC-new:SOT-23-6
- U7: value IT66121FN -> TPS2051BDGNR; device IC-new:QFN64-0.5-9X9MM -> IC-new:MSOP8-0.65-3X3MM
- U8: value ETA3410 -> TLV62569DBVT; device IC-new:DFN8G-0.5-2X2MM -> IC-new:SOT-23-5
- U9: value ESD-RCLAMP0524P -> SN74LVC1G125DCKR; device Discrete-new:ESD10P-0.5-2.5X1X0.58MM -> IC-new:SOT-353
- Y1: value ABS07-32.768KHZ-T -> CX3225GB24000P0HPQCC; device OSD3358-BSP Ref Design:CRYSTAL_3.2X1.5 -> OSD3358-BSP Ref Design:CRYSTAL-TXC-7A
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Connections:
- removed net N$14: C67.2, U3.1
- removed net N$26: L1.1, U5.2
- removed net N$3: C65.2, U3.7
- removed net N$53: R14.2, R9.1, U5.4
- removed net N$66: R69.1, U3.5
- removed net N$68: C76.1, L2.1, U3.3
- removed net N$71: C76.2, R69.2
- removed net N$73: R84.1, U3.8
- removed net N$74: C59.2, R84.2, R85.2, R93.2
- removed net N$78: R64.1, R94.1, U3.6
- new net N$77: R76.2, R78.2, U8.5
- new net N$79: L6.1, U8.3
- new net N$80: R76.1, R77.2
- new net N$84: R57.1, R58.2, U6.5
- new net N$86: C19.2, U6.6
- new net N$87: C19.1, L3.1, U6.2
- new net N$88: C23.1, R59.1, R60.2
- new net N$89: C23.2, R60.1, R61.2, U6.4
- net 1.8V-WIFI: now also C2.1, C7.2, C8.1, L1.2, R10.1, R30.1, R4.1, R6.1, R7.1, R8.1, R9.1, U4.38; no longer C52.2, C58.1, C64.1, FB6.2, MOD1.38, R100.1, R102.1, R103.1, R104.1, R111.1, R96.1, R97.1
- net 12VDC: now also C48.+, C51.+, C68.2, R97.2, U12.22, U12.28; no longer C70.+, C71.+, C73.2, IC1.22, IC1.28, R7.2
- net 3.3V-WIFI: now also C3.2, C4.1, C5.1, C6.1, L2.2, R11.2, R12.2, R5.2, U4.46, U4.47; no longer C39.1, C53.2, C57.1, C63.1, FB1.2, MOD1.46, MOD1.47, R114.2, R124.2, R125.2
- net AGND: now also C25.2, C27.2, C28.2, R66.2; no longer C10.2, C8.2, C9.2, R25.2
- net BT_EN: now also Q3.1, U4.41; no longer MOD1.41, T4.1
- net BT_HCI_CTS: now also R14.2; no longer R141.2
- net BT_HCI_RTS: now also R13.2; no longer R140.2
- net BT_HCI_RX: now also R16.2; no longer R143.2
- net BT_HCI_TX: now also R15.2; no longer R142.2
- net B_UART0_RX: now also J4.4, R80.2, U10.2; no longer J3.4, R27.2, U6.2
- net B_UART0_TX: now also J4.5, U10.3; no longer J3.5, U6.3
- net CEC: now also D12.1, J6.13, R106.2, U11.17; no longer D10.1, J4.13, R48.2, U7.17
- net CGND: now also C11.2, J1.P1, J1.P3, J1.P4, J1.P5, J1.P6, J3.G2, J6.PAD2, J6.PAD3, JP2.SG1, JP2.SG2, R48.2; no longer J5.G2, J5.G3, J5.G4, J8.P1, J8.P3, J8.P4, J8.P5, J8.P6, X2.5, X2.6
- net CK_N: now also J6.12, U11.21, U14.5, U14.6; no longer J4.12, U7.21, U9.5, U9.6
- net CK_P: now also J6.10, U11.22, U14.4, U14.7; no longer J4.10, U7.22, U9.4, U9.7
- net CLKOUT2: now also C37.2, R79.2, R96.2, U4.36; no longer C2.2, MOD1.36, R2.2, R3.2
- net COILA+: now also J5.1, U12.21; no longer IC1.21, J7.4, JP3.4, JP5.4
- net COILA-: now also J5.2, U12.24; no longer IC1.24, J7.3, JP3.3, JP5.3
- net COILB+: now also J5.4, U12.1; no longer IC1.1, J7.1, JP3.1, JP5.1
- net COILB-: now also J5.3, U12.26; no longer IC1.26, J7.2, JP3.2, JP5.2
- net CUR_REF: now also U12.17; no longer IC1.17, TP33.TP
- net D0_N: now also J6.9, U11.24, U14.2, U14.9; no longer J4.9, U7.24, U9.2, U9.9
- net D0_P: now also J6.7, U11.25, U14.1, U14.10; no longer J4.7, U7.25, U9.1, U9.10
- net D1_N: now also J6.6, U11.26, U13.5, U13.6; no longer J4.6, U11.5, U11.6, U7.26
- net D1_P: now also J6.4, U11.27, U13.4, U13.7; no longer J4.4, U11.4, U11.7, U7.27
- net D2_N: now also J6.3, U11.29, U13.2, U13.9; no longer J4.3, U11.2, U11.9, U7.29
- net D2_P: now also J6.1, U11.30, U13.1, U13.10; no longer J4.1, U11.1, U11.10, U7.30
- net DDC_SCL: now also D9.1, J6.15, R102.2, R104.2; no longer D12.1, J4.15, R43.2, R45.2
- net DDC_SDA: now also D10.1, J6.16, R103.2, R105.2; no longer D2.1, J4.16, R44.2, R46.2
- net DIR(GPIO23): now also R88.1, U12.19; no longer IC1.19, R78.1
- net EEPROM_WP: now also TP10.P1; no longer J1.1
- net ENABLE(GPIO46): now also R94.1, U12.2; no longer IC1.2, R77.1
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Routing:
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- added copper zone on layer 1, net 12VDC
- added copper zone on layer 15, net 12VDC
- added copper zone on layer 1, net 3.3V-WIFI
- added copper zone on layer 15, net CGND
- added copper zone on layer 16, net CGND
- added copper zone on layer 2, net CGND
- added copper zone on layer 1, net COILA+
- added copper zone on layer 16, net COILA+
- added copper zone on layer 1, net COILA-
- added copper zone on layer 16, net COILA-
- added copper zone on layer 1, net COILB+
- added copper zone on layer 16, net COILB+
- added copper zone on layer 1, net COILB-
- added copper zone on layer 16, net COILB-
- added copper zone on layer 15, net GND
- added copper zone on layer 16, net GND
- added copper zone on layer 2, net GND
- added copper zone on layer 1, net N$10
- added copper zone on layer 15, net N$14
- added copper zone on layer 2, net N$26
- added copper zone on layer 15, net N$3
- added copper zone on layer 15, net N$53
- added copper zone on layer 1, net N$55
- added copper zone on layer 16, net N$58
- added copper zone on layer 2, net N$66
- added copper zone on layer 15, net N$68
- added copper zone on layer 16, net N$71
- added copper zone on layer 1, net N$79
- added copper zone on layer 1, net N$86
- added copper zone on layer 1, net N$87
- added copper zone on layer 16, net N$87
- added copper zone on layer 1, net N$9
- added copper zone on layer 1, net PWR_IN_12V
- added copper zone on layer 15, net PWR_IN_12V
- added copper zone on layer 15, net SYS_RTC_1P8V
- added copper zone on layer 15, net SYS_VDD1_3P3V
- added copper zone on layer 15, net SYS_VDD3_3P3V
- added copper zone on layer 1, net VDD_3V3B
- added copper zone on layer 16, net VDD_3V3B
- added copper zone on layer 16, net VDD_5V
- added copper zone on layer 16, net VDD_USB_5V
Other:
- board text added: "1"
- board text added: "100ohm SINGLE ENDED IMPEDANCE CONTROL +/-10%"
- board text added: "4.5/5.5"
- board text added: "4.85/5.5"
- board text added: "50ohm SINGLE ENDED IMPEDANCE CONTROL +/-10%"
- board text added: "5V"
- board text added: "6"
- board text added: "90ohm SINGLE ENDED IMPEDANCE CONTROL +/-10%"
- board text added: "A+"
- board text added: "A-"
- board text added: "ANT1"
- board text added: "ANT2"
- board text added: "B+"
- board text added: "B-"
- board text added: "COPPER WEIGHT (OZ)"
- board text added: "DOUT"
- board text added: "Fan"
- board text added: "GND"
- board text added: "HALF+PLATING"
- board text added: "LAYER 1 - GTL"
- board text added: "LAYER 2 - GND"
- board text added: "LAYER 3 - POWER"
- board text added: "LAYER 4 - GBL"
- board text added: "LAYER STACK-UP - ALL DIMENSIONS IN MIL"
- board text added: "LAYER#"
- board text added: "LED"
- board text added: "Motor"
- board text added: "PWR"
- board text added: "RST"
- board text added: "RX"
- board text added: "TRACE WIDTH"
- board text added: "TRACE WIDTH / SPACE"
- board text added: "TX"
- board text added: "USR0"
- board text added: "USR1"
- board text added: "USR2"
- board text added: "USR3"

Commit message: Latest from Seeed
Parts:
- added R119: 10k, Discrete-new:R0402
- added U$1: (no value), logo:SEEED-SILK-TNAME-280*268MIL
- C84: value 1uF -> 1uF 10V
- R63: value 0R -> 10k
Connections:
- removed net AIN0: U1.A8
- removed net AIN1: U1.B8
- removed net AIN2: U1.B6
- removed net AIN3: U1.C6
- removed net AIN4: U1.C7
- removed net AIN5: U1.C8
- removed net AIN6: U1.C9
- removed net JTAG_EMU0: U1.E2
- removed net JTAG_EMU1: U1.E3
- removed net JTAG_TCK: U1.D1
- removed net JTAG_TDI: U1.C1
- removed net JTAG_TDO: U1.C2
- removed net JTAG_TMS: U1.D2
- removed net JTAG_TRSTN: U1.D3
- net BT_HCI_CTS: now also U1.D13; no longer U1.E13
- net BT_HCI_RTS: now also U1.E13; no longer U1.D13
- net BT_HCI_RX: now also U1.D15; no longer U1.D14
- net BT_HCI_TX: now also U1.D14; no longer U1.D15
- net CGND: now also J3.G3, J3.G4, J6.PAD, J6.PAD1
- net GND: now also R119.2
- net N$32: now also R119.1
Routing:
- net CGND: track 0.00 -> 238.2 mm, vias 68 -> 64
- net SYS_VDD1_3P3V: track 29.3 -> 200.3 mm, vias 19 -> 20
- net PWR_IN_12V: track 17.6 -> 23.6 mm
- net N$32: track 2.47 -> 6.20 mm
- net BT_HCI_TX: track 31.8 -> 34.8 mm
- net BT_HCI_RTS: track 36.8 -> 39.7 mm
- net BT_HCI_CTS: track 38.1 -> 35.4 mm
- net BT_HCI_RX: track 33.0 -> 30.9 mm
- net N$35: track 2.42 -> 4.20 mm
- net N$34: track 2.71 -> 4.49 mm
- net GND: track 207.4 -> 208.8 mm, vias 372 -> 377
- net BT_EN: track 49.7 -> 50.6 mm
- net CLKOUT2: track 85.3 -> 84.5 mm
- net N$29: track 3.18 -> 3.94 mm
- removed copper zone on layer 15, net N$14
- removed copper zone on layer 15, net SYS_VDD1_3P3V
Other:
- board text added: "12Vdc 4A input"
- board text added: "Whitherbone"
- board text added: "v1.0 09/07/2018"
